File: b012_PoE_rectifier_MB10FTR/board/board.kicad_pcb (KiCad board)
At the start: 2 copper layers, 21 x 13 mm, 4 parts, among them J1 004_BASE-T_CT_2x3, J2 PoE_2x2

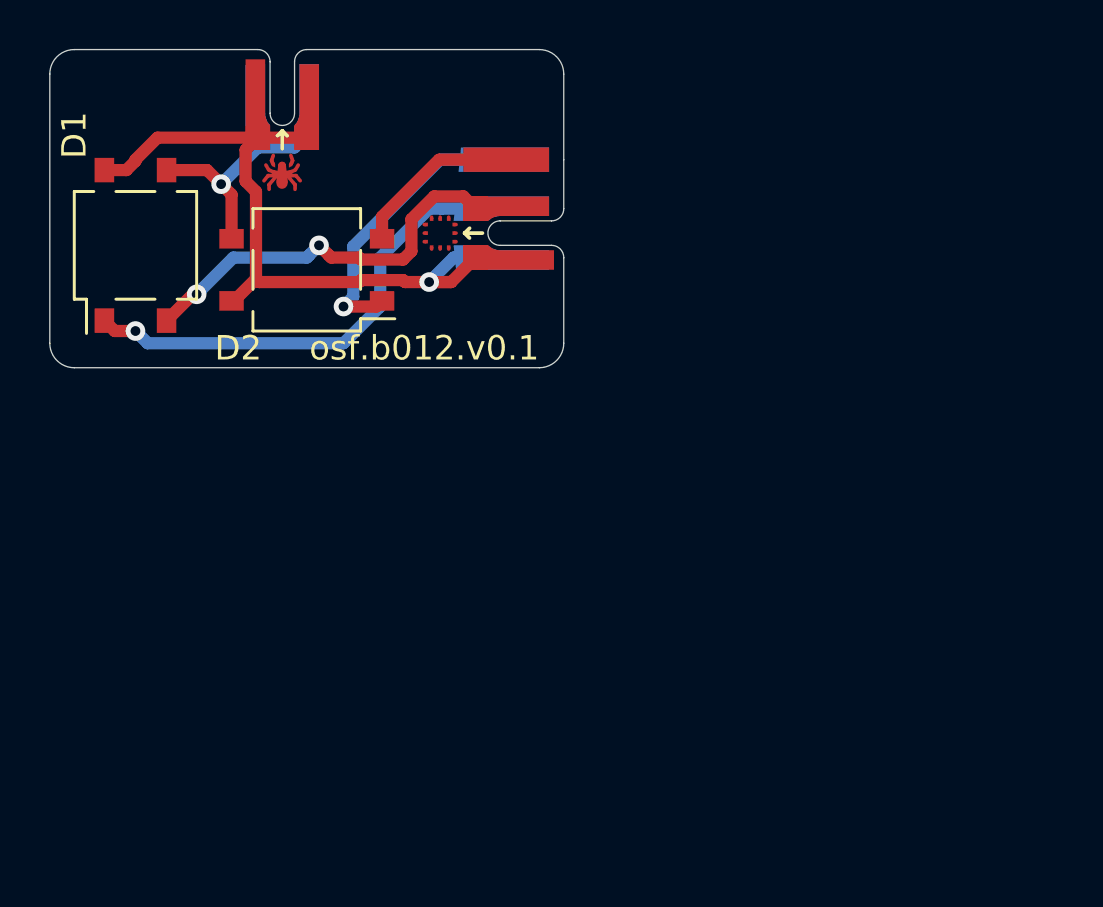
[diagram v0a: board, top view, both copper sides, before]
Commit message: updated connectors
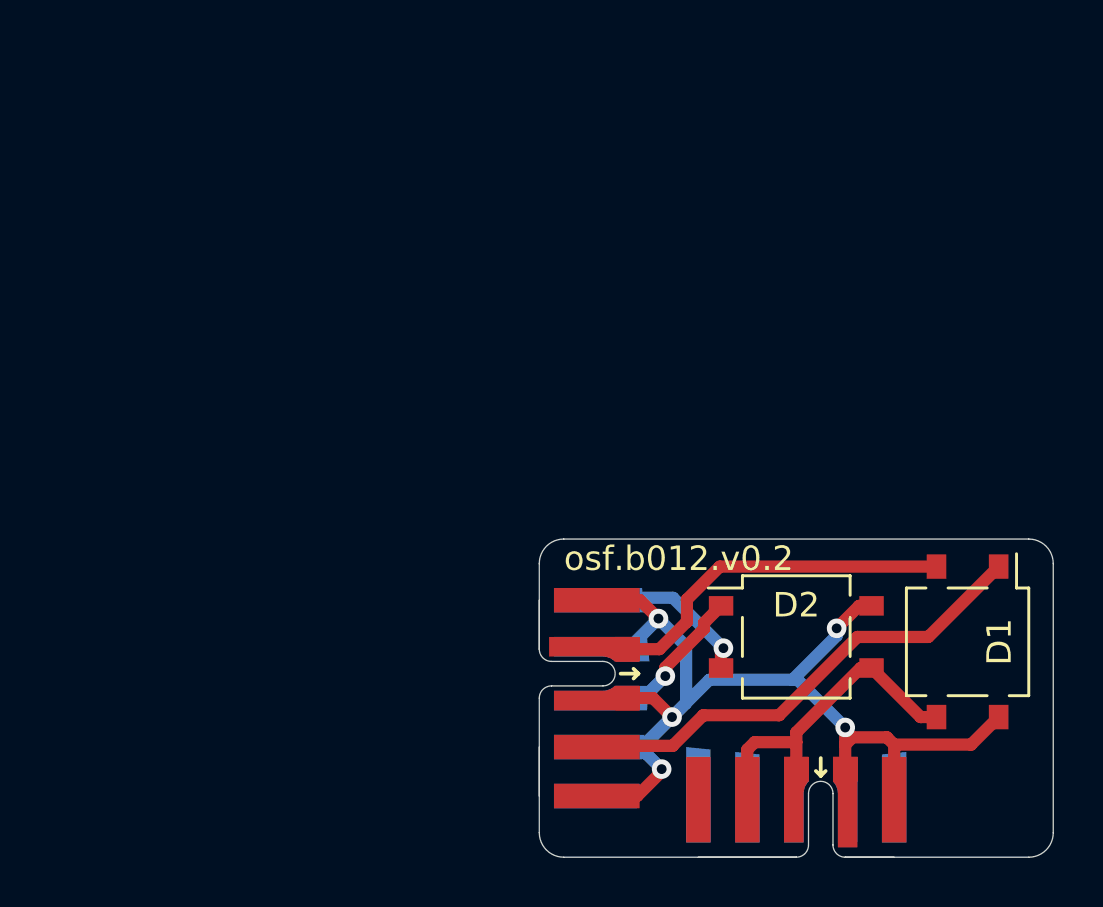
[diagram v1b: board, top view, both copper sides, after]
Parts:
- J1: footprint on_edge:on_edge_2x03_device -> on_edge:on_edge_2x05_device
- J2: footprint on_edge:on_edge_2x02_host -> on_edge:on_edge_2x05_host
- moved J2 38.6 mm to (150.5, 113.0), turned to 180 degrees
- moved D1 37.7 mm to (157.5, 104.2), turned to 270 degrees
- moved D2 25.0 mm to (150.5, 104.0), turned to 0 degrees
- moved J1 20.0 mm to (140.0, 106.5), turned to 270 degrees
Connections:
- J1 pad 5: Net-(D2-Pad2) -> GND
- J1 pad 6: Net-(D2-Pad1) -> Net-(D2-Pad2)
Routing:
- net GND: track 30.6 -> 46.6 mm, vias 1 -> 5
- net Net-(D2-Pad1): track 12.0 -> 7.24 mm
- net Net-(D1-Pad2): track 16.2 -> 14.6 mm, vias 2 -> 0
- net Net-(D1-Pad1): track 20.5 -> 19.5 mm, vias 1 -> 0
- net Net-(D1-Pad3): track 12.5 -> 13.3 mm, vias 1 -> 0
- net Net-(D2-Pad2): track 6.94 -> 6.87 mm, vias 0 -> 1
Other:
- outline, holes or cut-outs redrawn
- board text added: "osf.b012.v0.2"
- board text removed: "osf.b012.v0.1"

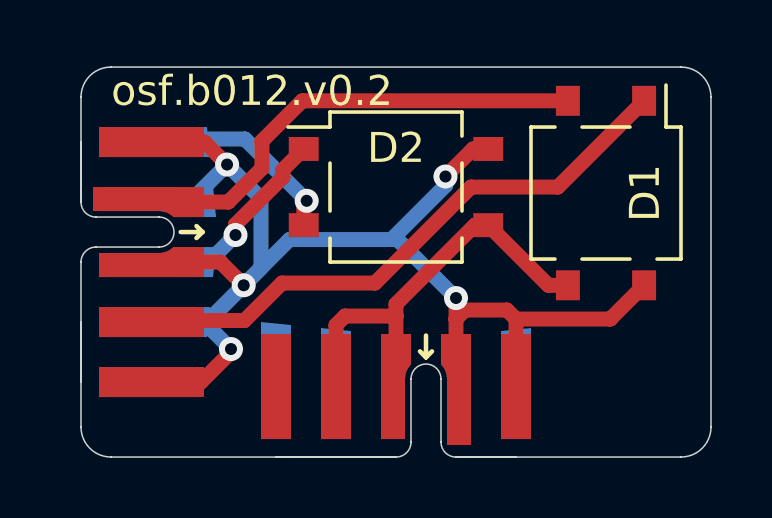
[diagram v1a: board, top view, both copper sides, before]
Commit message: changed to horizontal style
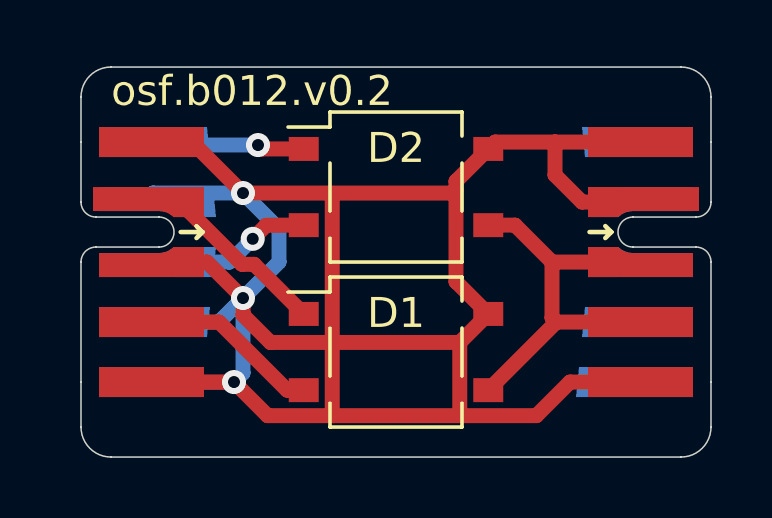
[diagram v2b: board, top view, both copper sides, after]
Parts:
- moved J2 12.3 mm to (161.0, 106.5), turned to 270 degrees
- moved D1 8.78 mm to (150.5, 109.5), turned to 0 degrees
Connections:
- J1 pad 2: Net-(D1-Pad2) -> Net-(D1-Pad1)
- J1 pad 4: Net-(D1-Pad1) -> Net-(D1-Pad2)
- J1 pad 6: Net-(D2-Pad2) -> Net-(D2-Pad1)
- J1 pad 8: Net-(D2-Pad1) -> Net-(D2-Pad2)
- J2 pad 5: (no net) -> GND
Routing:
- net GND: track 46.6 -> 81.5 mm, vias 5 -> 3
- net Net-(D1-Pad1): track 19.5 -> 5.55 mm
- net Net-(D1-Pad2): track 14.6 -> 6.02 mm
- net Net-(D2-Pad1): track 7.24 -> 5.12 mm
- net Net-(D2-Pad2): track 6.87 -> 5.83 mm
- net Net-(D1-Pad3): track 13.3 -> 12.4 mm
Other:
- outline, holes or cut-outs redrawn
